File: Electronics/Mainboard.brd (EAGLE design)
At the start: 100 x 80 mm, 35 parts, among them IC1 4081N, IC2 4069N, Q1 IRFZ48V, Q2 IRF4905V, Q3 IRFZ48V, Q4 IRF4905V, Q5 IRFZ48V, Q6 IRF4905V, Q7 IRFZ48V, Q8 IRF4905V, X3 24V Batt

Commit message: Arduino sofware, updated electronics and some report outline.
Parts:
- removed C1: (no value), rcl:E7,5-18
- added C2: (no value), rcl:E5-10,5
- added LED1: (no value), led:LED5MM
- added R13: 1k, rcl:0207/10
- R10, R11, R12, R7, R8, R9: value (none) -> 180
- moved JP1 70.1 mm to (53.3, 43.2), turned to 90 degrees
- moved JP3 66.5 mm to (57.1, 10.2), turned to 90 degrees
- moved U$1 61.9 mm to (59.7, -16.5), turned to 90 degrees
- moved R12 58.6 mm to (95.2, 22.9), turned to 90 degrees
- moved R11 55.1 mm to (91.4, 22.9), turned to 90 degrees
- moved R10 50.9 mm to (87.6, 22.9), turned to 90 degrees
- moved IC2 49.3 mm to (68.6, 17.8)
- moved IC1 43.2 mm to (87.6, 10.2), turned to 0 degrees
- moved R9 25.9 mm to (85.1, 22.9), turned to 90 degrees
- moved R8 21.7 mm to (81.3, 22.9), turned to 90 degrees
- moved R7 18.2 mm to (76.2, 22.9), turned to 90 degrees
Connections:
- net N$35 renamed +3V3
- removed net N$29: C1.-, OK1.3, OK2.3, OK3.3, OK4.3, OK5.3, OK6.3, Q1.S, Q3.S, Q5.S, Q7.S, X3.2
- removed net N$30: C1.+, Q2.S, Q4.S, Q6.S, Q8.S, R1.2, R2.2, R3.2, R4.2, R5.2, R6.2, X3.1
- new net +24V: C2.+, LED1.A, Q2.S, Q4.S, Q6.S, Q8.S, R1.2, R2.2, R3.2, R4.2, R5.2, R6.2, X3.1
- new net GND2: C2.-, OK1.3, OK2.3, OK3.3, OK4.3, OK5.3, OK6.3, Q1.S, Q3.S, Q5.S, Q7.S, R13.1, X3.2
- new net N$41: JP1.3
- new net N$42: JP1.4
- new net N$6: LED1.K, R13.2
- net N$26: no longer JP1.4
- net N$37: no longer JP1.3
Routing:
- net GND2: track 0.00 -> 267.4 mm
- net N$29: track 265.5 -> 0.00 mm
- net N$10: track 0.00 -> 185.6 mm
- net N$7: track 0.00 -> 173.1 mm
- net N$27: track 0.00 -> 152.3 mm
- net +24V: track 0.00 -> 144.2 mm
- net N$11: track 0.00 -> 141.2 mm
- net N$30: track 129.3 -> 0.00 mm
- net GND: track 0.00 -> 120.2 mm
- net VCC: track 0.00 -> 34.2 mm
- net N$16: track 0.00 -> 34.2 mm
- net N$39: track 0.00 -> 23.2 mm
- net N$17: track 0.00 -> 19.4 mm
- net N$15: track 0.00 -> 13.0 mm, vias 1 -> 0
- net N$25: track 0.00 -> 11.7 mm
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
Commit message: 
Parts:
- removed C2: (no value), rcl:E5-10,5
- removed IC2: 4069N, 40xx:DIL14
- removed LED1: (no value), led:LED5MM
- removed OK1, OK2, OK3, OK4, OK5, OK6: PC817, optocoupler:DIL04
- removed Q1, Q3, Q5, Q7: IRFZ48V, transistor-power:TO220BV
- removed Q2, Q4, Q6, Q8: IRF4905V, transistor-power:TO220BV
- removed R1, R2, R3, R4, R5, R6: 10k, rcl:0207/10
- removed R11, R12: 180, rcl:0207/10
- removed R13: 1k, rcl:0207/10
- removed X1, X2: (no value), con-wago-508:W237-132
- removed X3: 24V Batt, con-wago-508:W237-132
- added JP2: Motorcontroller, pinhead:2X05
- added JP5: Display, pinhead:2X07
- added T1, T2: BC547, transistor:TO92
- JP1: device pinhead:1X06 -> pinhead:2X07
- R10, R9: value 180 -> 1k
- R7, R8: value 180 -> 10k
- moved U$1 75.5 mm to (-14.0, 0.00), turned to 0 degrees
- moved R9 71.2 mm to (14.0, 19.1), turned to 0 degrees
- moved R10 48.9 mm to (44.5, 45.7), turned to 0 degrees
- moved IC1 48.2 mm to (41.9, 25.4)
- moved R7 45.8 mm to (30.5, 25.4)
- moved R8 42.6 mm to (40.6, 35.6), turned to 180 degrees
- moved JP1 34.9 mm to (41.9, 10.2), turned to 0 degrees
- moved JP3 27.1 mm to (30.5, 5.08), turned to 180 degrees
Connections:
- removed net +24V: C2.+, LED1.A, Q2.S, Q4.S, Q6.S, Q8.S, R1.2, R2.2, R3.2, R4.2, R5.2, R6.2, X3.1
- removed net GND2: C2.-, OK1.3, OK2.3, OK3.3, OK4.3, OK5.3, OK6.3, Q1.S, Q3.S, Q5.S, Q7.S, R13.1, X3.2
- removed net N$12: OK1.4, Q1.G, Q2.G, R1.1
- removed net N$13: OK3.4, Q3.G, R3.1
- removed net N$14: OK3.1, R9.2
- removed net N$15: IC1.3, R8.1
- removed net N$18: Q7.D, Q8.D, X2.1
- removed net N$19: OK4.4, Q7.G, Q8.G, R4.1
- removed net N$21: OK5.4, Q6.G, R5.1
- removed net N$22: OK6.4, Q5.G, R6.1
- removed net N$23: OK6.1, R12.2
- removed net N$24: IC1.10, R11.1
- removed net N$25: IC1.11, R12.1
- removed net N$27: IC1.12, IC2.3, R10.1, U$1.D4
- removed net N$28: OK1.1, R7.2
- removed net N$6: LED1.K, R13.2
- removed net N$9: OK2.4, Q4.G, R2.1
- removed net VCC: IC1.14, IC2.14, U$1.5V
- new net +5V: IC1.14, JP5.2, R7.2, R8.2, U$1.5V
- new net N$31: JP5.4, U$1.D6
- new net N$38: JP5.8, U$1.D8
- new net N$40: JP5.10, U$1.D9
- new net N$43: JP5.14, U$1.D11
- new net N$44: JP5.3, U$1.D12
- new net N$45: JP5.5, U$1.D13
- new net N$46: JP5.7, U$1.A3
- net GND: now also JP1.3, JP2.10, JP5.1, T1.1, T2.1; no longer IC2.7, JP1.2, OK1.2, OK2.2, OK3.2, OK4.2, OK5.2, OK6.2
- net N$1: now also IC1.3, JP2.2; no longer Q5.D, Q6.D, X2.2
- net N$10: now also JP2.1, R9.1; no longer IC2.1, R7.1
- net N$16: now also R8.1, T2.3; no longer IC2.4
- net N$17: now also R9.2, T1.2; no longer IC1.4, R9.1
- net N$2: now also IC1.4, JP2.3; no longer Q3.D, Q4.D, X1.1
- net N$20: now also R10.2, T2.2; no longer OK5.1, R11.2
- net N$26: now also JP1.7
- net N$3: now also IC1.12, JP2.4, R10.1, U$1.D4; no longer OK2.1, R8.2
- net N$37: now also JP5.6, U$1.D7; no longer U$1.A4
- net N$4: now also IC1.10, JP2.5; no longer Q1.D, Q2.D, X1.2
- net N$41: now also JP1.5, U$1.A4; no longer JP1.3
- net N$42: now also JP5.12, U$1.D10; no longer JP1.4
- net N$5: now also IC1.11, JP2.6; no longer OK4.1, R10.2
- net N$8: now also R7.1, T1.3; no longer IC2.2
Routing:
- net GND2: track 267.4 -> 0.00 mm
- net N$13: track 165.4 -> 0.00 mm, vias 1 -> 0
- net N$27: track 152.3 -> 0.00 mm
- net +24V: track 144.2 -> 0.00 mm
- net N$7: track 173.1 -> 29.8 mm, vias 0 -> 1
- net N$9: track 141.7 -> 0.00 mm, vias 2 -> 1
- net N$12: track 101.9 -> 0.00 mm, vias 2 -> 1
- net N$11: track 141.2 -> 42.7 mm
- net N$21: track 93.8 -> 0.00 mm, vias 1 -> 0
- net N$46: track 0.00 -> 93.2 mm
- net N$10: track 185.6 -> 94.1 mm
- net +5V: track 0.00 -> 76.8 mm
- net N$22: track 64.8 -> 0.00 mm
- net N$3: track 9.94 -> 61.7 mm
- net N$19: track 47.0 -> 0.00 mm, vias 2 -> 0
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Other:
- board size 100 x 80 mm -> 68.6 x 53.3 mm
- board text added: "1"
- board text added: "24 jan 2012"
- board text added: "Carl-Emil Grøn Christensen & Mathias Dannesbo"
- board text added: "Display"
- board text added: "Gyro"
- board text added: "Mainboard v1.0"
- board text added: "Motor"
- board text added: "Swagway"

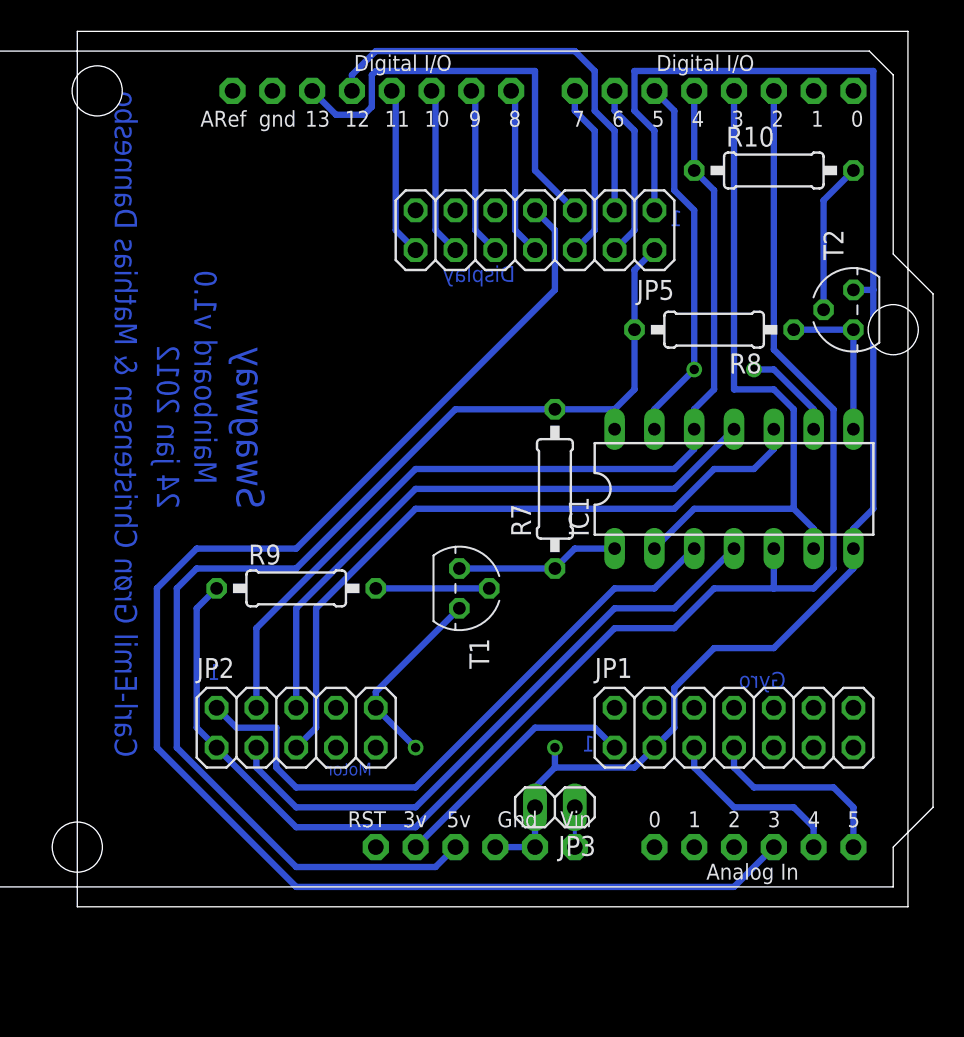
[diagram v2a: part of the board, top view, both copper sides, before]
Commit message: Mainboard 2.0. Fixes #1, #2 #12
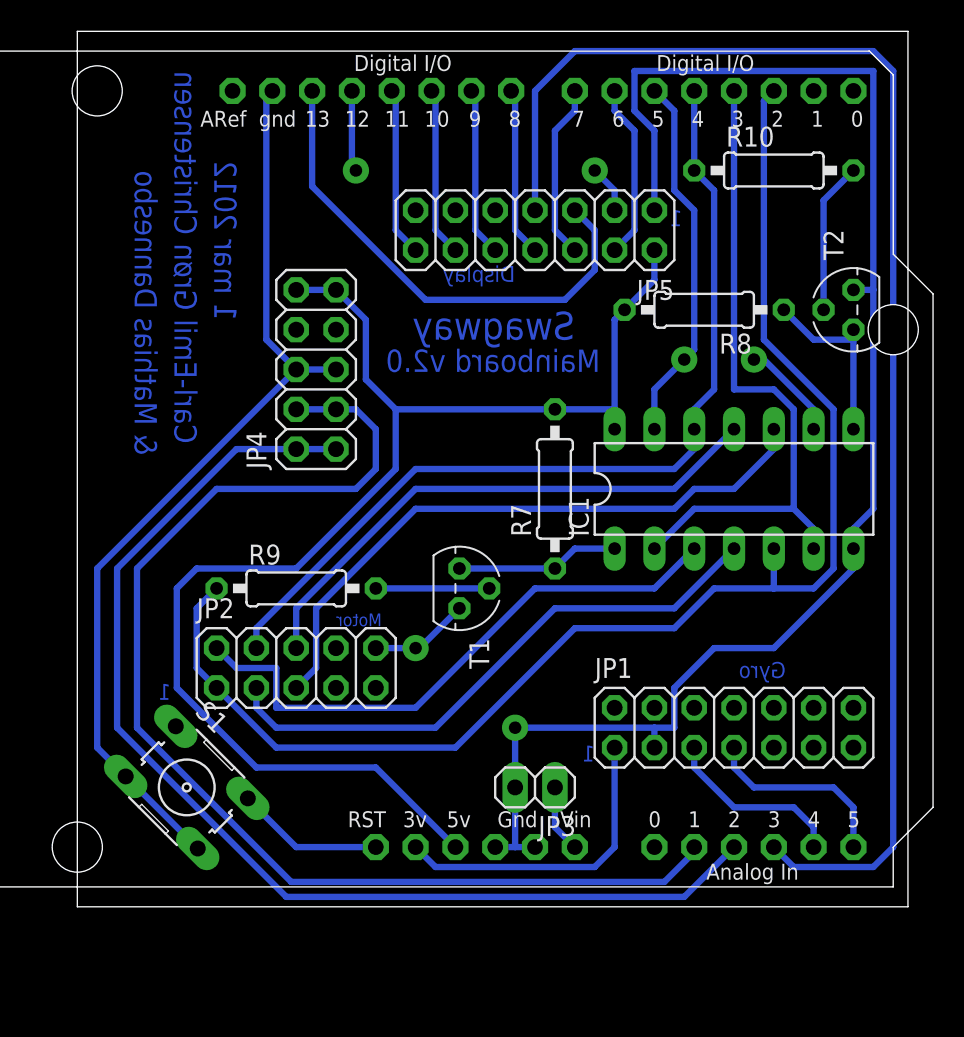
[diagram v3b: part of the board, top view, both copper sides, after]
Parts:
- added JP4: Steering, pinhead:2X05
- added S1: (no value), switch-omron:B3F-10XX
- moved JP2 3.81 mm to (14.0, 14.0)
- moved JP3 1.80 mm to (29.2, 6.35)
- moved R8 1.42 mm to (40.0, 36.8)
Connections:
- new net N$13: JP4.3, JP4.4, U$1.A1
- new net N$14: JP4.1, JP4.2, U$1.A2
- new net N$15: S1.2, U$1.RESET
- net +5V: now also JP4.10, JP4.9
- net GND: now also JP4.5, JP4.6, S1.4
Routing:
- net N$13: track 0.00 -> 76.9 mm
- net N$14: track 0.00 -> 72.4 mm
- net GND: track 105.6 -> 163.1 mm
- net N$44: track 27.1 -> 8.25 mm, vias 0 -> 1
- net +5V: track 76.8 -> 87.5 mm
- net N$15: track 0.00 -> 9.57 mm
- net N$10: track 94.1 -> 88.2 mm
- net N$45: track 27.1 -> 32.3 mm
- net N$5: track 39.0 -> 35.2 mm
- net N$4: track 44.1 -> 40.3 mm
- net N$3: track 61.7 -> 57.9 mm
- net +3V3: track 16.4 -> 20.1 mm
- net N$46: track 93.2 -> 90.3 mm
- net N$2: track 39.6 -> 37.0 mm
- net N$1: track 40.4 -> 37.8 mm
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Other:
- board text added: "& Mathias Dannesbo"
- board text added: "1 mar 2012"
- board text added: "Carl-Emil Grøn Christensen"
- board text added: "Mainboard v2.0"
- board text removed: "24 jan 2012"
- board text removed: "Carl-Emil Grøn Christensen & Mathias Dannesbo"
- board text removed: "Mainboard v1.0"

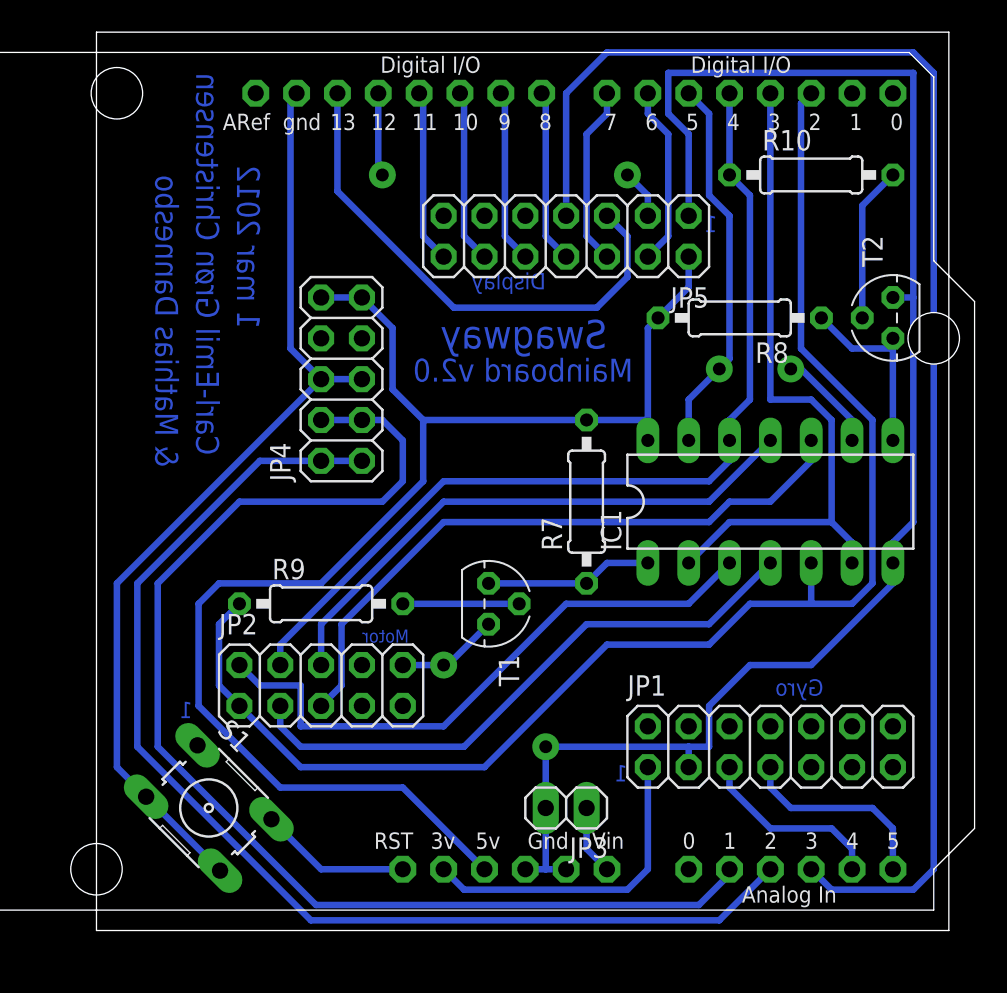
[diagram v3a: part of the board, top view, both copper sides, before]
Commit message: New mainboard. Closes #13, closes #21 and closes #9 as it becomes irrelevant.
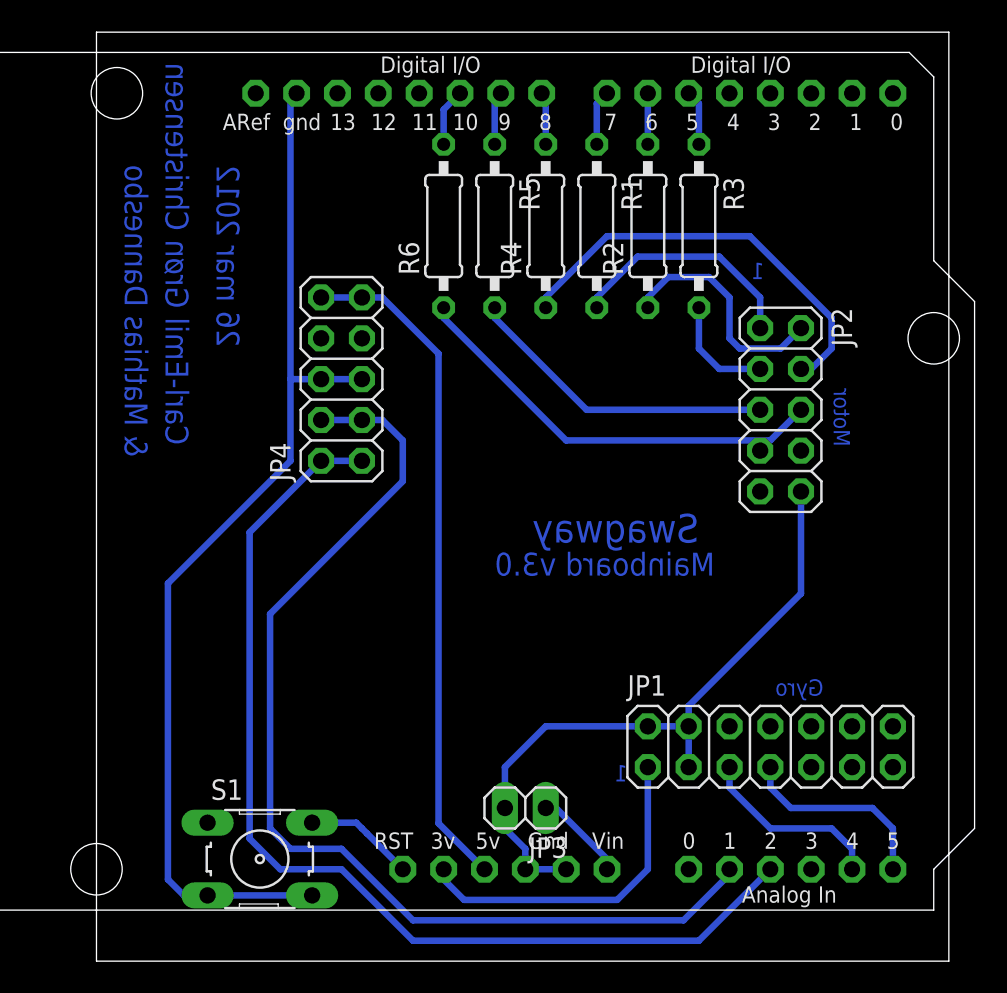
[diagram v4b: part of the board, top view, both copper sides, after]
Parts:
- removed IC1: 4081N, 40xx:DIL14
- removed JP5: Display, pinhead:2X07
- removed R10, R9: 1k, rcl:0207/10
- removed R7, R8: 10k, rcl:0207/10
- removed T1, T2: BC547, transistor:TO92
- added R1, R2, R3, R4, R5, R6: 330R, rcl:0207/10
- moved JP2 33.3 mm to (42.5, 31.1), turned to 270 degrees
- moved S1 4.49 mm to (10.2, 3.17), turned to 0 degrees
- moved JP3 2.54 mm to (26.7, 6.35)
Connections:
- removed net N$20: R10.2, T2.2
- removed net N$31: JP5.4, U$1.D6
- removed net N$37: JP5.6, U$1.D7
- removed net N$38: JP5.8, U$1.D8
- removed net N$40: JP5.10, U$1.D9
- removed net N$42: JP5.12, U$1.D10
- removed net N$43: JP5.14, U$1.D11
- removed net N$44: JP5.3, U$1.D12
- removed net N$45: JP5.5, U$1.D13
- removed net N$46: JP5.7, U$1.A3
- new net N$6: JP2.6, R6.1
- net +5V: no longer IC1.14, JP5.2, R7.2, R8.2
- net GND: no longer IC1.7, JP5.1, T1.1, T2.1
- net N$1: now also JP2.1, R1.2; no longer IC1.3, JP2.2
- net N$10: now also R2.2, U$1.D6; no longer IC1.5, JP2.1, R9.1, U$1.D2
- net N$11: now also R4.2, U$1.D8; no longer IC1.2, IC1.6, U$1.D3
- net N$16: now also R5.1, U$1.D9; no longer IC1.8, R8.1, T2.3
- net N$17: now also R6.2, U$1.D10; no longer R9.2, T1.2
- net N$2: now also R3.2; no longer IC1.4
- net N$3: now also JP2.5, R5.2; no longer IC1.12, JP2.4, R10.1, U$1.D4
- net N$4: now also JP2.2, R2.1; no longer IC1.10, JP2.5
- net N$5: now also JP2.4, R4.1; no longer IC1.11, JP2.6
- net N$7: now also R1.1, U$1.D7; no longer IC1.13, IC1.9, U$1.D5
- net N$8: now also R3.1, U$1.D5; no longer IC1.1, R7.1, T1.3
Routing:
- net N$46: track 90.3 -> 0.00 mm
- net N$10: track 88.2 -> 3.17 mm
- net GND: track 163.1 -> 108.0 mm
- net +5V: track 87.5 -> 42.0 mm
- net N$11: track 42.7 -> 3.28 mm
- net N$3: track 57.9 -> 19.5 mm
- net N$45: track 32.3 -> 0.00 mm
- net N$2: track 37.0 -> 6.88 mm
- net N$6: track 0.00 -> 26.8 mm
- net N$7: track 30.1 -> 3.44 mm
- net N$4: track 40.3 -> 14.5 mm
- net N$1: track 37.8 -> 14.8 mm
- net N$13: track 76.9 -> 65.6 mm
- net N$31: track 11.2 -> 0.00 mm
- net N$37: track 11.2 -> 0.00 mm
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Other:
- board text added: "26 mar 2012"
- board text added: "Mainboard v3.0"
- board text removed: "1 mar 2012"
- board text removed: "Display"
- board text removed: "Mainboard v2.0"
